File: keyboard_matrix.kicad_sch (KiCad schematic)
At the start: 16 parts, among them SW10 SW_Push_Dual, SW3 SW_Push_Dual, SW4 SW_Push_Dual, SW5 SW_Push_Dual, SW6 SW_Push_Dual, SW7 SW_Push_Dual, SW8 SW_Push_Dual, SW9 SW_Push_Dual

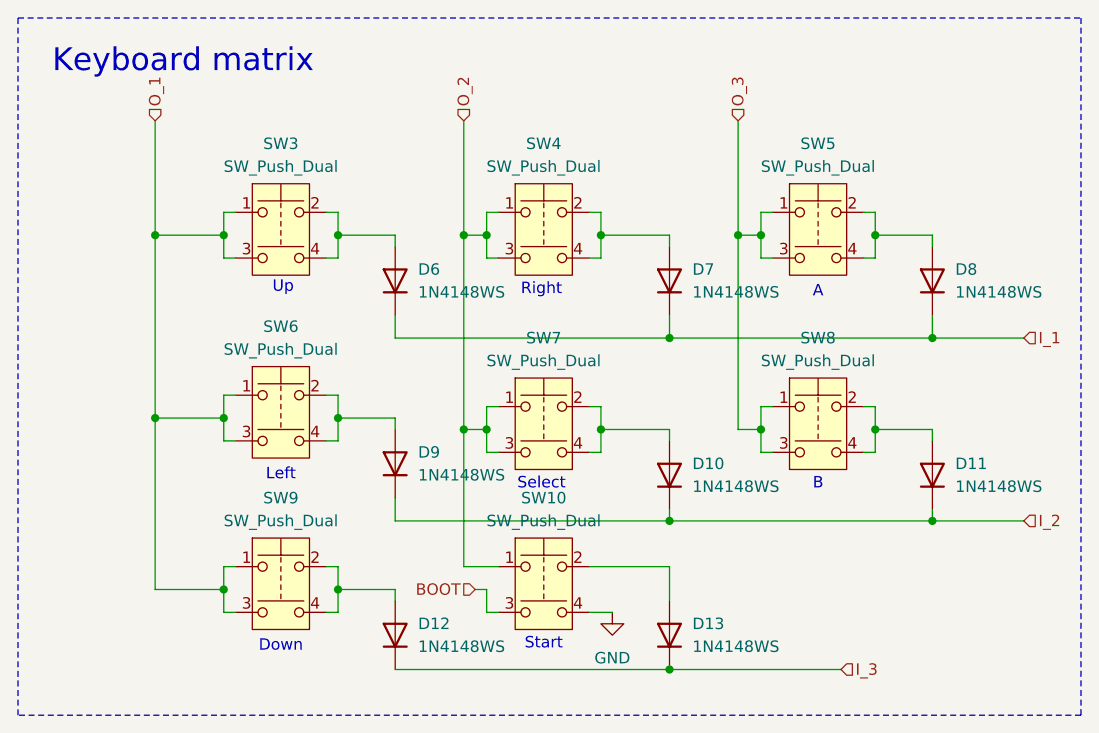
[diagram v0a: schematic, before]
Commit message: Bugs fixed (buttons and OLED holes)
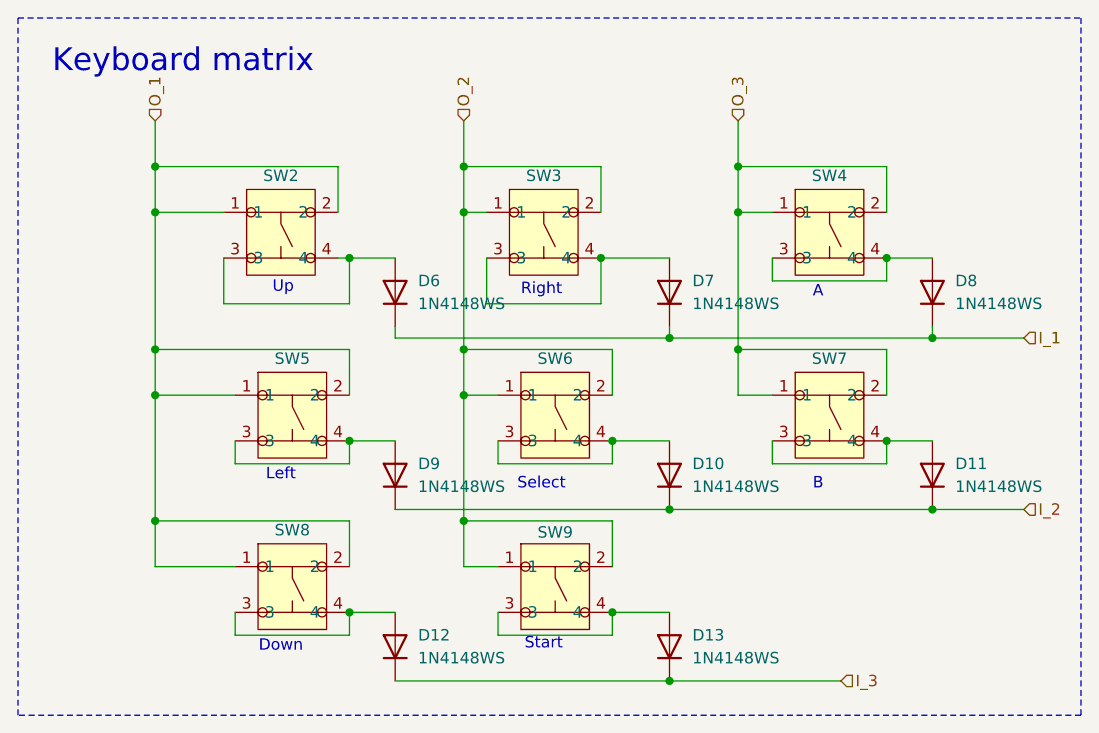
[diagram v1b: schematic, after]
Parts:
- removed SW10, SW3, SW4, SW5, SW6, SW7, SW8, SW9: SW_Push_Dual, footprints:PTS526SM15SMTR2LFS, symbol Switch:SW_Push_Dual
- added SW2, SW3, SW4, SW5, SW6, SW7, SW8, SW9: PTS526_SK15_SMTR2_LFS, footprints:PTS526SK15SMTR2LFS, symbol PTS526_SK15_SMTR2_LFS:PTS526_SK15_SMTR2_LFS
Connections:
- net O_1: now also SW2.1, SW2.2, SW5.1, SW5.2, SW8.1, SW8.2
- net O_2: now also SW3.1, SW3.2, SW6.1, SW6.2, SW9.1, SW9.2
- net O_3: now also SW4.1, SW4.2, SW7.1, SW7.2
- net at D6.2 (A): now also SW2.3, SW2.4
- net at D7.2 (A): now also SW3.3, SW3.4
- net at D13.2 (A): now also SW9.3, SW9.4
- net at D10.2 (A): now also SW6.3, SW6.4
- net at D12.2 (A): now also SW8.3, SW8.4
- net at D9.2 (A): now also SW5.3, SW5.4
- net at D8.2 (A): now also SW4.3, SW4.4
- net at D11.2 (A): now also SW7.3, SW7.4
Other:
- moved on the sheet: D12, D13, D6, D7, D8, D9
